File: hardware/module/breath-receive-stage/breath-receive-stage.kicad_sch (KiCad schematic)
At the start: 17 parts

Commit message: WIP module schematics: footprints, bought-part fields, and the two board projects (module-main, module-jack)
Recovered from a container restart; not yet exported or checked.

Co-Authored-By: Claude Opus 5.5 <noreply@anthropic.com>
Claude-Session: https://claude.ai/code/session_01LmB4muFXnoLprWX4JzuJ5A
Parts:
- C-CM-IN+, C-CM-IN-: footprint (none) -> Capacitor_SMD:C_0805_2012Metric; Assembly (none) -> machine; LCSC (none) -> C541572; MPN (none) -> CC0805FRNPO9BN152; Manufacturer (none) -> YAGEO
- C-DEC-INAMP-NEG, C-DEC-INAMP-POS, C-DEC-REFBUF-NEG, C-DEC-REFBUF-POS: footprint (none) -> Capacitor_SMD:C_0805_2012Metric; Assembly (none) -> machine; LCSC (none) -> C49678; MPN (none) -> CC0805KRX7R9BB104; Manufacturer (none) -> YAGEO
- C-DIFF-BREATH: footprint (none) -> Capacitor_SMD:C_0805_2012Metric; Assembly (none) -> machine; LCSC (none) -> C445728; MPN (none) -> C2012C0G1H153JT000N; Manufacturer (none) -> TDK
- D-CLAMP-IN+, D-CLAMP-IN-: footprint (none) -> Package_TO_SOT_SMD:SOT-23; Assembly (none) -> machine; LCSC (none) -> C2500; MPN (none) -> BAV99,215; Manufacturer (none) -> Nexperia
- R-GAIN-INAMP: footprint (none) -> Resistor_SMD:R_0805_2012Metric; Assembly (none) -> machine; LCSC (none) -> C706241; MPN (none) -> RT0805BRD0742K2L; Manufacturer (none) -> YAGEO
- R2, R3: footprint (none) -> Resistor_SMD:R_0805_2012Metric; Assembly (none) -> machine; LCSC (none) -> C110775; MPN (none) -> RT0805BRD0710KL; Manufacturer (none) -> YAGEO
- R4, R5: footprint (none) -> Resistor_SMD:R_0805_2012Metric; Assembly (none) -> machine; LCSC (none) -> C17514; MPN (none) -> 0805W8F1004T5E; Manufacturer (none) -> UNI-ROYAL(Uniroyal Elec)
- TRIM-BREATH-ZERO: footprint (none) -> Potentiometer_THT:Potentiometer_Bourns_3296W_Vertical; Assembly (none) -> hand; LCSC (none) -> C34846; MPN (none) -> 3296W-1-103LF; Manufacturer (none) -> Bourns
- U-DIFFRX: footprint (none) -> Package_SO:SOIC-8_3.9x4.9mm_P1.27mm; Assembly (none) -> machine; LCSC (none) -> C544342; MPN (none) -> INA828IDR; Manufacturer (none) -> Texas Instruments
- U-REF-BUF: footprint (none) -> Package_SO:SOIC-8_3.9x4.9mm_P1.27mm; Assembly (none) -> machine; LCSC (none) -> C139363; MPN (none) -> OPA2197IDR; Manufacturer (none) -> Texas Instruments

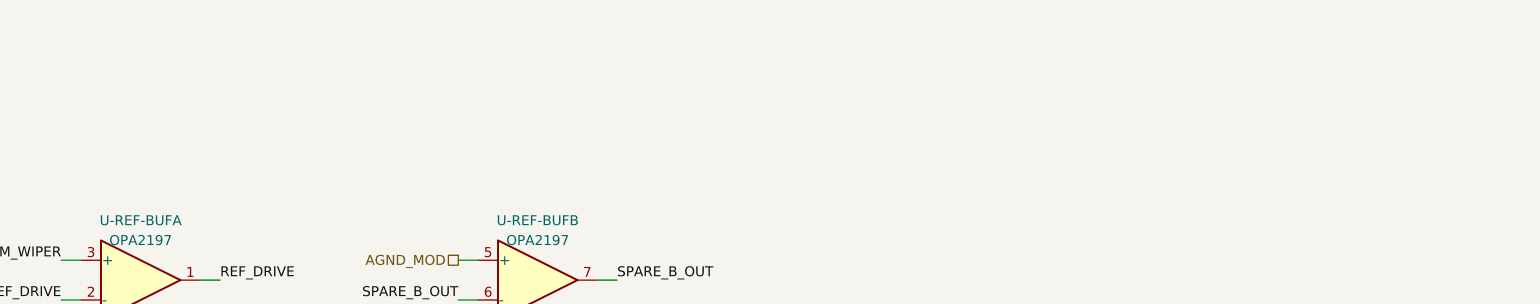
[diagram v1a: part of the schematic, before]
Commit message: Module schematics: the ten circuits' netlists exported from their sheets; J-B2B-MOD allocated by position
- Every module circuit's netlist.yaml is now EXPORTED from its KiCad sheet
  (ADR 0019), identical part by part and net by net to the hand-written one,
  including its foreign: parts. kicad.py exports foreign: from FOREIGN lines of
  sheet text; without it the breath receive page's R1 went unresolved.
- J-B2B-MOD, re-allocated: the pots' nets on the top rows (the pots sit above
  the header), each side's pot and jacks in its own column, a ground on the
  diagonal of every other row so every signal but the LED's +12 V has a ground
  pin beside it.
- kicad.py check: J-B2B-MOD is one conductor per pin on both module boards, and
  the main board's etherCON matches hardware/interfaces/spi-link pin for pin.
- sch.py: a board's sub-sheet pin with one member is a no-connect again (the
  interfaces' spare-label rule assumed a part pin).

Co-Authored-By: Claude Opus 5.5 <noreply@anthropic.com>
Claude-Session: https://claude.ai/code/session_01LmB4muFXnoLprWX4JzuJ5A
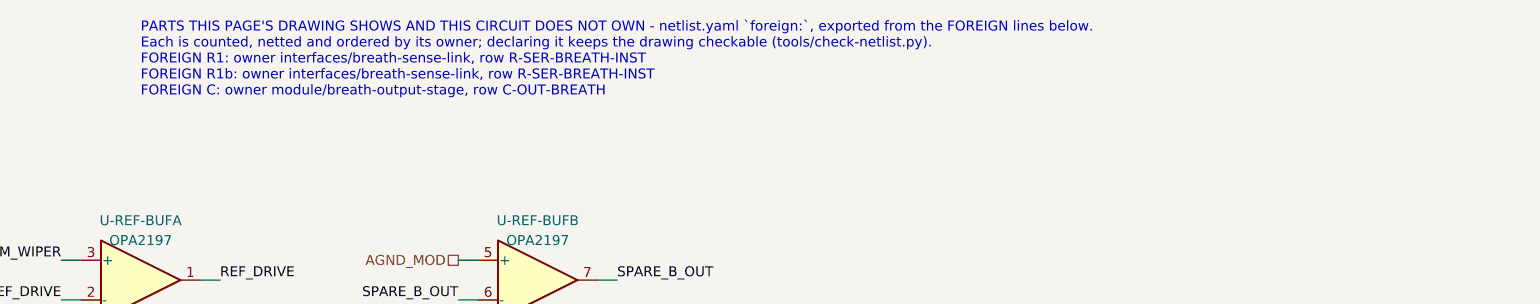
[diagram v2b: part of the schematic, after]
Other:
- note added: "PARTS THIS PAGE'S DRAWING SHOWS AND THIS CIRCUIT DOES NOT OWN - netlist.yaml `foreign:`, exported from the FOREIGN lines below. Each is counted, netted and ordered by its owner; declaring it keeps the drawing checkable (tools/check-netlist.py). FOREIGN R1: owner interfaces/breath-sense-link, row R-SER-BREATH-INST FOREIGN R1b: owner interfaces/breath-sense-link, row R-SER-BREATH-INST FOREIGN C: ow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"
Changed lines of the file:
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@@
   (label "SPARE_B_OUT" (at 81.28 53.34 180) (fields_autoplaced) (effects (font (size 1.27 1.27)) (justify right bottom)))
   (text "FROM THE HAND-WRITTEN NETLIST THIS SHEET REPLACES (verbatim; the part notes are on each part's Note field):\n\nAUTHORITATIVE for connectivity. The ASCII drawing in breath-receive-stage.md is a REPRESENTATION of this file.\n\nSCOPE. That drawing spans two boards deliberately - it shows the sensor, its buffer and R1/R1b at the\ninstrument end so the differential pole and the CMRR budget can be derived in one place. THOSE PARTS ARE NOT\nTHIS CIRCUIT'S and are not components here; they arrive as ports. The same is true of the output stage block\nat the bottom, which is module/breath-output-stage.\n\nParts this page DRAWS for context and does not own. The drawing spans two boards on purpose, so R1/R1b and the\nsensor appear in it; they are interfaces/breath-sense-link's rows and must not be counted, netted or ordered\nhere. Declaring them keeps the drawing checkable without pretending they are ours.\n\n[of] qty 2: R2 and R3 are the two instances\n\n[of] qty 2: R4 and R5\n\n[of] qty 2, one per leg\n\n[drawn_as] the drawing spells a subscript with _\n\n[drawn_as] both legs carry the same label and value\n\n[of] qty 2, one per input leg\n\n[U-REF-BUF] ONE OPA2197 PACKAGE. Half A buffers the trimmer wiper into the in-amp's REF; half B is one of the\nmodule's two spare halves (breath-output-stage.md: \"ten of twelve halves used across the module, two spare\"),\ntied off as a follower on the star so it cannot oscillate or rail.\n\n[SPARE_B_OUT] The spare half's follower loop." (at 408.94 38.099999999999994 0) (effects (font (size 1.27 1.27)) (justify left top)))
+  (text "PARTS THIS PAGE'S DRAWING SHOWS AND THIS CIRCUIT DOES NOT OWN - netlist.yaml `foreign:`, exported from the FOREIGN lines below.\nEach is counted, netted and ordered by its owner; declaring it keeps the drawing checkable (tools/check-netlist.py).\nFOREIGN R1: owner interfaces/breath-sense-link, row R-SER-BREATH-INST\nFOREIGN R1b: owner interfaces/breath-sense-link, row R-SER-BREATH-INST\nFOREIGN C: owner module/breath-output-stage, row C-OUT-BREATH" (at 40.64 17.78 0) (effects (font (size 1.27 1.27)) (justify left top)))
   (sheet_instances (path "/" (page "1")))
 )

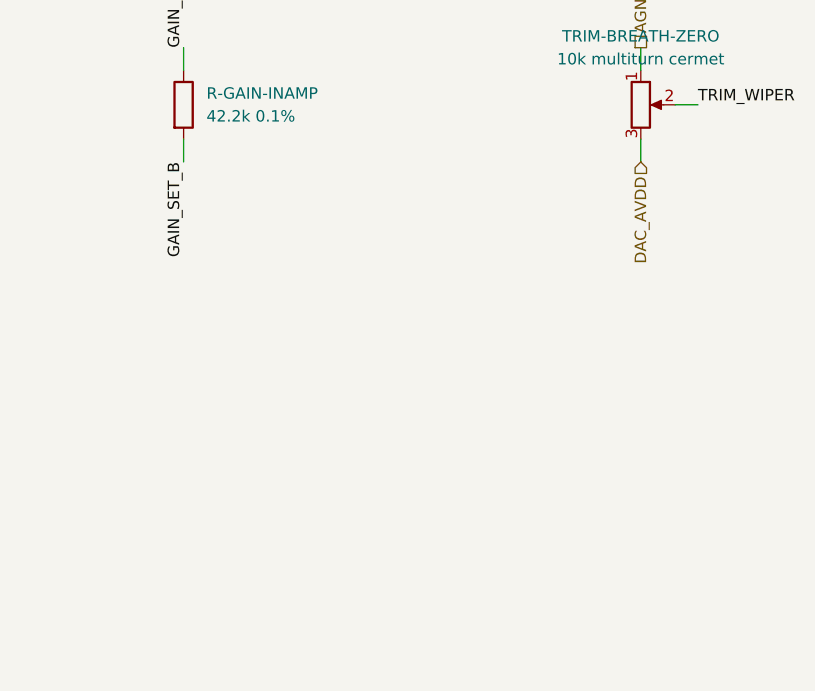
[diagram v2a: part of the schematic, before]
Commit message: Module: D3 turned round; pitch trims made buildable and bipolar; LT5400 pad and order code; breath-zero range resistor
D3 (the -12 V entry diode) was netlisted anode-to-bus, reverse-biased in
normal running (found by the analog sims): cathode to the bus now.
TRIM-OFFSET spans VREFOUT-AGND and injects through R-VREF-INJ against
R-VREF-SER into the follower at gain 1.02 (R-VREF-FB/R-VREF-GND): 2.500 V at
mid-travel, -60/+50 mV. It also holds the 3-state VREFOUT at 0 V while the
DAC's reference is disabled. TRIM-GAIN is centred by R-GAIN-CTR in the R1 leg
(+/-1 %) and its CW end strapped to the wiper. RN-PITCH carries its exposed
pad as pin 9 to AGND_MOD, spares tied down; ordered LT5400BIMS8E-1#PBF.
R-OPAMP-IN is six; R-TRIM-RANGE split into real parts. R-ZERO-TOP gives
TRIM-BREATH-ZERO the 0-1.0 V range its page specifies. Page text follows.

Co-Authored-By: Claude Opus 5.5 <noreply@anthropic.com>
Claude-Session: https://claude.ai/code/session_01LmB4muFXnoLprWX4JzuJ5A
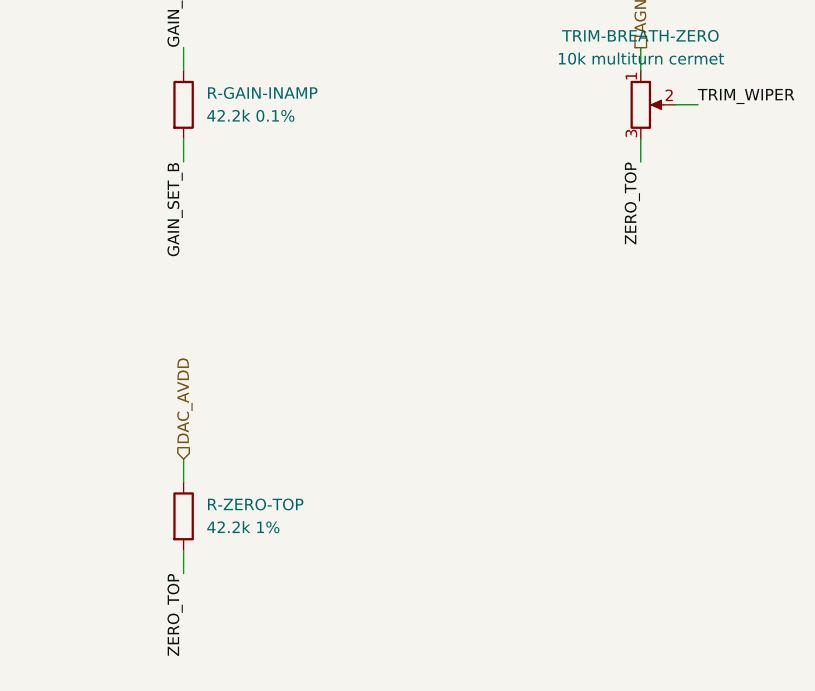
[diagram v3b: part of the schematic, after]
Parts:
- added R-ZERO-TOP: 42.2k 1%, Resistor_SMD:R_0805_2012Metric, symbol Device:R
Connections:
- net DAC_AVDD: now also R-ZERO-TOP.1; no longer TRIM-BREATH-ZERO.3
- new net ZERO_TOP: R-ZERO-TOP.2, TRIM-BREATH-ZERO.3
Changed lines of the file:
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@@
     (property "Figure" "inamp-full-scale" (at 256.54 243.84 0) (effects (font (size 1.27 1.27)) hide)))
   (wire (pts (xy 91.44 328.93) (xy 91.44 331.47)) (stroke (width 0) (type default)))
-  (hierarchical_label "DAC_AVDD" (shape input) (at 91.44 331.47 270) (effects (font (size 1.27 1.27)) (justify right))
-    (property "Dir" "in" (at 91.44 331.47 0) (effects (font (size 1.27 1.27)) hide))
-    (property "From" "module/power-entry" (at 91.44 331.47 0) (effects (font (size 1.27 1.27)) hide))
-    (property "Figure" "dac-rail" (at 91.44 331.47 0) (effects (font (size 1.27 1.27)) hide)))
+  (label "ZERO_TOP" (at 91.44 331.47 270) (fields_autoplaced) (effects (font (size 1.27 1.27)) (justify right bottom)))
   (wire (pts (xy 243.84 236.22) (xy 243.84 233.68)) (stroke (width 0) (type default)))
   (hierarchical_label "MODULE_ANALOG_POS12" (shape input) (at 243.84 233.68 90) (effects (font (size 1.27 1.27)) (justify left))
@@
   (text "FROM THE HAND-WRITTEN NETLIST THIS SHEET REPLACES (verbatim; the part notes are on each part's Note field):\n\nAUTHORITATIVE for connectivity. The ASCII drawing in breath-receive-stage.md is a REPRESENTATION of this file.\n\nSCOPE. That drawing spans two boards deliberately - it shows the sensor, its buffer and R1/R1b at the\ninstrument end so the differential pole and the CMRR budget can be derived in one place. THOSE PARTS ARE NOT\nTHIS CIRCUIT'S and are not components here; they arrive as ports. The same is true of the output stage block\nat the bottom, which is module/breath-output-stage.\n\nParts this page DRAWS for context and does not own. The drawing spans two boards on purpose, so R1/R1b and the\nsensor appear in it; they are interfaces/breath-sense-link's rows and must not be counted, netted or ordered\nhere. Declaring them keeps the drawing checkable without pretending they are ours.\n\n[of] qty 2: R2 and R3 are the two instances\n\n[of] qty 2: R4 and R5\n\n[of] qty 2, one per leg\n\n[drawn_as] the drawing spells a subscript with _\n\n[drawn_as] both legs carry the same label and value\n\n[of] qty 2, one per input leg\n\n[U-REF-BUF] ONE OPA2197 PACKAGE. Half A buffers the trimmer wiper into the in-amp's REF; half B is one of the\nmodule's two spare halves (breath-output-stage.md: \"ten of twelve halves used across the module, two spare\"),\ntied off as a follower on the star so it cannot oscillate or rail.\n\n[SPARE_B_OUT] The spare half's follower loop." (at 408.94 38.099999999999994 0) (effects (font (size 1.27 1.27)) (justify left top)))
   (text "PARTS THIS PAGE'S DRAWING SHOWS AND THIS CIRCUIT DOES NOT OWN - netlist.yaml `foreign:`, exported from the FOREIGN lines below.\nEach is counted, netted and ordered by its owner; declaring it keeps the drawing checkable (tools/check-netlist.py).\nFOREIGN R1: owner interfaces/breath-sense-link, row R-SER-BREATH-INST\nFOREIGN R1b: owner interfaces/breath-sense-link, row R-SER-BREATH-INST\nFOREIGN C: owner module/breath-output-stage, row C-OUT-BREATH" (at 40.64 17.78 0) (effects (font (size 1.27 1.27)) (justify left top)))
+  (symbol (lib_id "Device:R") (at 40.64 370.84 0) (unit 1)
+    (in_bom yes) (on_board yes) (dnp no)
+    (property "Reference" "R-ZERO-TOP" (at 43.18 369.57 0) (effects (font (size 1.27 1.27)) (justify left)))
+    (property "Value" "42.2k 1%" (at 43.18 372.11 0) (effects (font (size 1.27 1.27)) (justify left)))
+    (property "Footprint" "Resistor_SMD:R_0805_2012Metric" (at 40.64 370.84 0) (effects (font (size 1.27 1.27)) hide))
+    (property "Datasheet" "" (at 40.64 370.84 0) (effects (font (size 1.27 1.27)) hide))
+    (property "Row" "R-ZERO-TOP" (at 40.64 370.84 0) (effects (font (size 1.27 1.27)) hide))
+    (property "Pins" "1=1 2=2" (at 40.64 370.84 0) (effects (font (size 1.27 1.27)) hide))
+    (property "Note" "Top of TRIM-BREATH-ZERO's divider: 42.2k over the 10k track spans the wiper 0 to 0.998 V of DAC_AVDD, the 0 to +1.0 V the page specifies, so breath-zero-ref sits at mid-track rather than a tenth of the way up" (at 40.64 370.84 0) (effects (font (size 1.27 1.27)) hide))
+    (property "Manufacturer" "UNI-ROYAL(Uniroyal Elec)" (at 40.64 370.84 0) (effects (font (size 1.27 1.27)) hide))
+    (property "MPN" "0805W8F4222T5E" (at 40.64 370.84 0) (effects (font (size 1.27 1.27)) hide))
+    (property "LCSC" "C17686" (at 40.64 370.84 0) (effects (font (size 1.27 1.27)) hide))
+    (property "Assembly" "machine" (at 40.64 370.84 0) (effects (font (size 1.27 1.27)) hide))
+    (pin "1")
+    (pin "2")
+    (instances (project "module-main" (path "/fc77e9f9-9171-5c83-92ae-8cafe880764e/b9269a67-5d3e-5ef8-9f1e-1a172d05979c" (reference "R66") (unit 1))) (project "breath-receive-stage" (path "/22139c3e-7ede-5820-8fb6-f1f51a9f74b0" (reference "R-ZERO-TOP") (unit 1))))
+  )
+  (wire (pts (xy 40.64 367.03) (xy 40.64 364.49)) (stroke (width 0) (type default)))
+  (hierarchical_label "DAC_AVDD" (shape input) (at 40.64 364.49 90) (effects (font (size 1.27 1.27)) (justify left))
+    (property "Dir" "in" (at 40.64 364.49 0) (effects (font (size 1.27 1.27)) hide))
+    (property "From" "module/power-entry" (at 40.64 364.49 0) (effects (font (size 1.27 1.27)) hide))
+    (property "Figure" "dac-rail" (at 40.64 364.49 0) (effects (font (size 1.27 1.27)) hide)))
+  (wire (pts (xy 40.64 374.65) (xy 40.64 377.19)) (stroke (width 0) (type default)))
+  (label "ZERO_TOP" (at 40.64 377.19 270) (fields_autoplaced) (effects (font (size 1.27 1.27)) (justify right bottom)))
   (sheet_instances (path "/" (page "1")))
 )

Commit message: Owner decisions D1, D2, D3, D5, CMRR: the parts on the sheets (#11, #14, #15, #16, #5, #12)
The owner's choices of 2026-10-03 (working chat), applied to the KiCad sheets,
exported, rendered, and carried into the BOM fragments:

- D1 (#11 F2, #14 A1, #12-3), "10 ohm + 22 uF + 10 uF": breath-adc gains
  R-ADC-VDD (10R 1% 0805, UNI-ROYAL 0805W8F100JT5E, C17415, JLC basic) from
  DEV_3V3 to a new local net ADC_VDD = U-ADC pin 8, with C-ADC-VDD (22 uF
  X5R 25 V 1206, Samsung CL31A226KAHNNNE, C12891, JLC basic) beside the
  existing C-ADC-BULK and C-DEC-ADC (C3 kept); a PWR_FLAG on ADC_VDD for
  ERC. power-entry-instrument gains C-BUCK-OUT (10 uF X5R 50 V 1206,
  Samsung CL31A106KBHNNNE, C13585, JLC basic) at U-BUCK-A's OUT (main-board
  U5, the R-78E5.0 - RECOM's standard application, #14 A1 item 3).
  Main board: R47, C42, C43.
- D5: U-ADC CH1 tied to AGND_INST.
- D2 (#15 C2, #16 B2), "Yes, all 4 channels": a second SP0504BAHTG at J5
  on CHAIN_SCK, CHAIN_SHLD, HOP_LT_RH, HOP_RH_RT - main-board U11 on the
  root sheet, U-TVS-CHAIN-RH on the key-chain-loom sheet; row qty 2.
- D3 (#15 C3): R-SPI-SER (R1-R3) Panasonic ERJ-P08F82R0V (C4065013, 0 at
  JLC and LCSC; in-stock equivalent Vishay CRCW120682R0FKEAHP, C1854869,
  named in the row); R-SER-BREATH-INST (R38/R39) ERJ-P08F1001V (C4261071,
  JLC 4,299).
- CMRR (#5-5), "Tighten cap matching": C-CM-BREATH a matched pair, each
  within 0.5 % of the pair's mean, from one reel of the 1 % C0G, measured
  and hand-fitted (no 1.5 nF C0G is catalogued tighter than 1 %).

Banked: Samsung CL31A226KAHNNNE and CL31A106KBHNNNE spec sheets, Vishay
CRCW-HP e3 (fragment .manifest-R51-owner-decisions.csv). Also two module
sims the deff676 merge staled and these changes do not touch (panel-led,
digital-and-supervision) re-run: 0 failed.

Gate-Red: sims staled by these netlists are re-running in the next commits; main-board .kicad_pcb awaits wave-3 placement of R47, C42, C43, U11 (and fab/ renders); known stale photos/clash

Co-Authored-By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
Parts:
- C-CM-IN+, C-CM-IN-: Assembly machine -> hand; Note (none) -> A MATCHED PAIR with its twin (owner, 2026-10-03: 'Tighten c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
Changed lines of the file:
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@@
     (property "MPN" "CC0805FRNPO9BN152" (at 243.84 187.96 0) (effects (font (size 1.27 1.27)) hide))
     (property "LCSC" "C541572" (at 243.84 187.96 0) (effects (font (size 1.27 1.27)) hide))
-    (property "Assembly" "machine" (at 243.84 187.96 0) (effects (font (size 1.27 1.27)) hide))
+    (property "Assembly" "hand" (at 243.84 187.96 0) (effects (font (size 1.27 1.27)) hide))
+    (property "Note" "A MATCHED PAIR with its twin (owner, 2026-10-03: 'Tighten cap matching'): C-CM-IN+ and C-CM-IN- from one reel of the 1 % C0G part, measured on one LCR meter at 1 kHz and fitted together only when each is within 0.5 % of the pair's mean. Their mismatch converts the umbilical's common mode in proportion to frequency, and at 1 % each the link misses its CMRR at the breath band's top (module/breath-receive-stage/sim cmrr-as-netlisted). No catalogue C0G at 1.5 nF is sold tighter than 1 %, so the match is made by hand: fitted by hand, after measuring" (at 243.84 187.96 0) (effects (font (size 1.27 1.27)) hide))
     (pin "1")
     (pin "2")
@@
     (property "MPN" "CC0805FRNPO9BN152" (at 294.64 187.96 0) (effects (font (size 1.27 1.27)) hide))
     (property "LCSC" "C541572" (at 294.64 187.96 0) (effects (font (size 1.27 1.27)) hide))
-    (property "Assembly" "machine" (at 294.64 187.96 0) (effects (font (size 1.27 1.27)) hide))
+    (property "Assembly" "hand" (at 294.64 187.96 0) (effects (font (size 1.27 1.27)) hide))
+    (property "Note" "A MATCHED PAIR with its twin (owner, 2026-10-03: 'Tighten cap matching'): C-CM-IN+ and C-CM-IN- from one reel of the 1 % C0G part, measured on one LCR meter at 1 kHz and fitted together only when each is within 0.5 % of the pair's mean. Their mismatch converts the umbilical's common mode in proportion to frequency, and at 1 % each the link misses its CMRR at the breath band's top (module/breath-receive-stage/sim cmrr-as-netlisted). No catalogue C0G at 1.5 nF is sold tighter than 1 %, so the match is made by hand: fitted by hand, after measuring" (at 294.64 187.96 0) (effects (font (size 1.27 1.27)) hide))
     (pin "1")
     (pin "2")
